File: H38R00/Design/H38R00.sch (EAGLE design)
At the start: 1 part, among them P1 HEXABIT_17.32_X2_POWER_ONLY

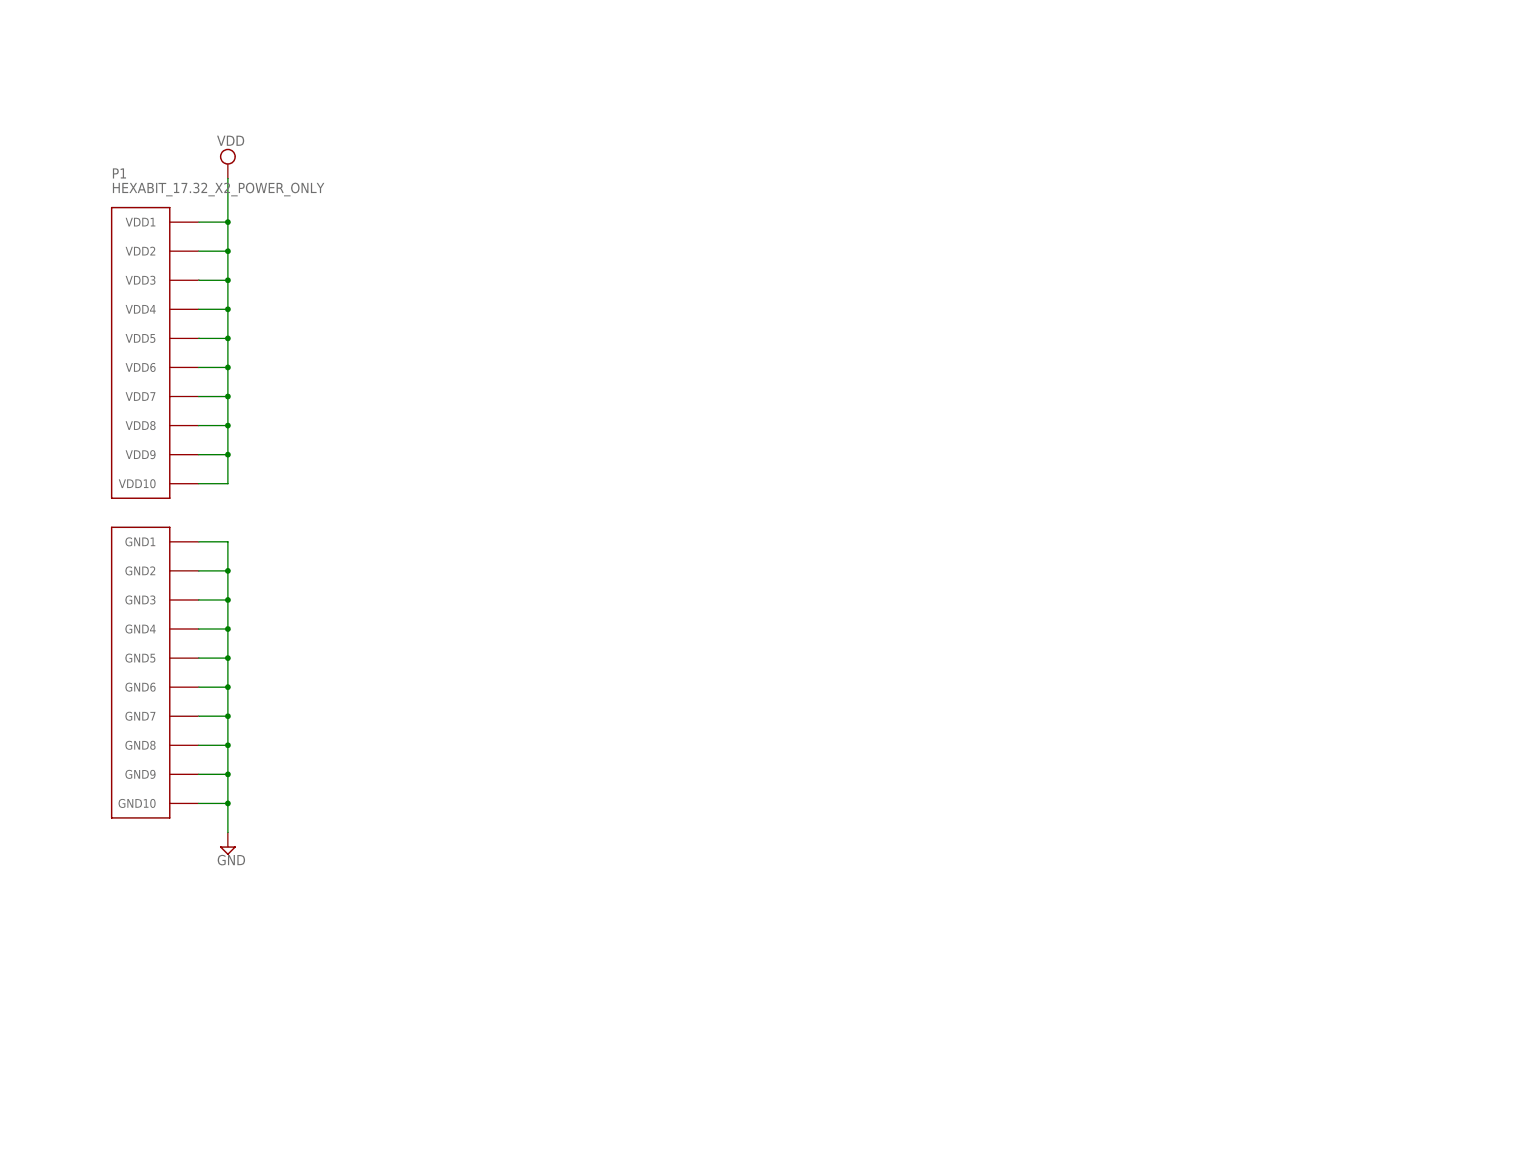
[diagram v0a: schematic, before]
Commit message: Added main ICs and some passives
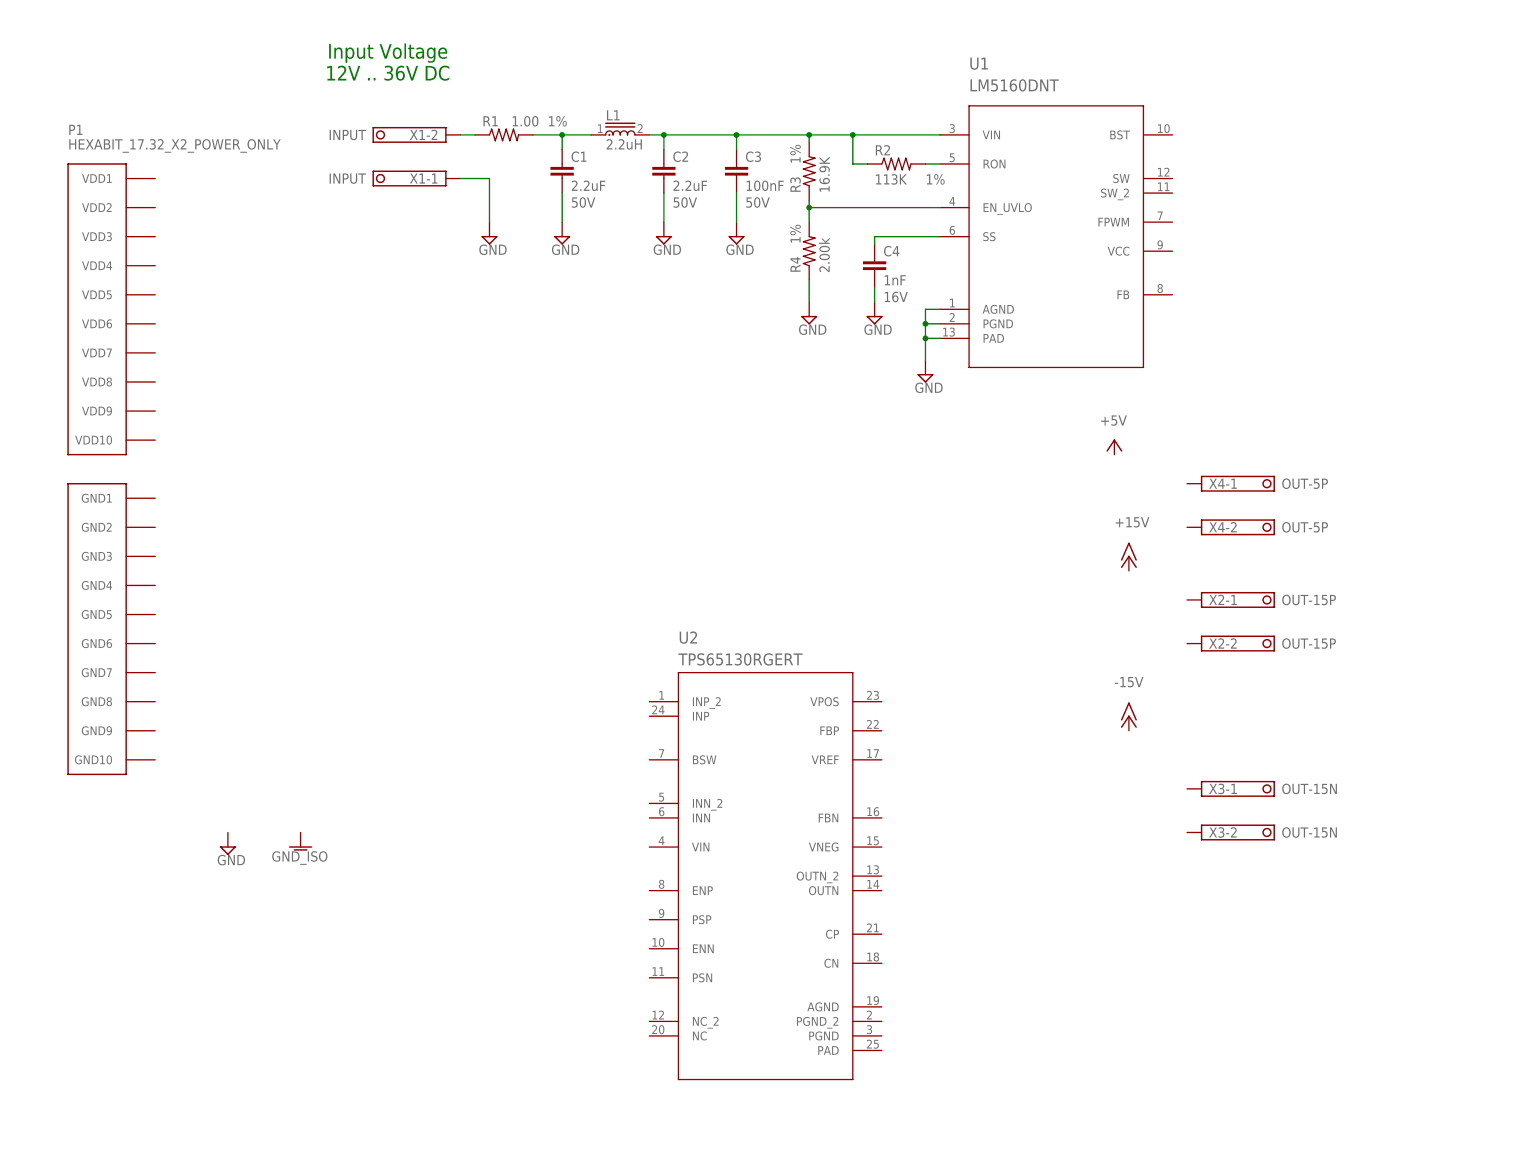
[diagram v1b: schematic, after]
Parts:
- added C1, C2: 2.2uF, Hexabitz:C-1206
- added C3: 100nF, Hexabitz:C-0603
- added C4: 1nF, Hexabitz:C-0603
- added L1: 2.2uH, Hexabitz:LQM18PN2R2MFHD
- added R1: 1.00, Hexabitz:R-0603
- added R2: 113K, Hexabitz:R-0603
- added R3: 16.9K, Hexabitz:R-0603
- added R4: 2.00k, Hexabitz:R-0603
- added U1: LM5160DNT, Hexabitz:LM5160DNT
- added U2: TPS65130RGERT, Hexabitz:TPS65130RGERT
- added X1: INPUT, Hexabitz:CON-PHOENIX-350_1751248
- added X2: OUT-15P, Hexabitz:CON-PHOENIX-350_1751248
- added X3: OUT-15N, Hexabitz:CON-PHOENIX-350_1751248
- added X4: OUT-5P, Hexabitz:CON-PHOENIX-350_1751248
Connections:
- removed net VDD: P1.VDD1, P1.VDD10, P1.VDD2, P1.VDD3, P1.VDD4, P1.VDD5, P1.VDD6, P1.VDD7, P1.VDD8, P1.VDD9
- new net N$1: R1.1, X1-2.K
- new net N$2: C1.1, L1.1, R1.2
- new net N$3: C2.1, C3.1, L1.2, R2.1, R3.2, U1.VIN
- new net N$4: R2.2, U1.RON
- new net N$5: R3.1, R4.2, U1.EN_UVLO
- new net N$6: C4.1, U1.SS
- net GND: now also C1.2, C2.2, C3.2, C4.2, R4.1, U1.AGND, U1.PAD, U1.PGND, X1-1.K; no longer P1.GND1, P1.GND10, P1.GND2, P1.GND3, P1.GND4, P1.GND5, P1.GND6, P1.GND7, P1.GND8, P1.GND9
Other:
- note added: "Input Voltage 12V .. 36V DC"
- note added: "Isolated +/-15V DC-DC Power"
- note removed: "Bipolar +/-15V DC-DC Power"
- moved on the sheet: P1

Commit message: Finished the buck part
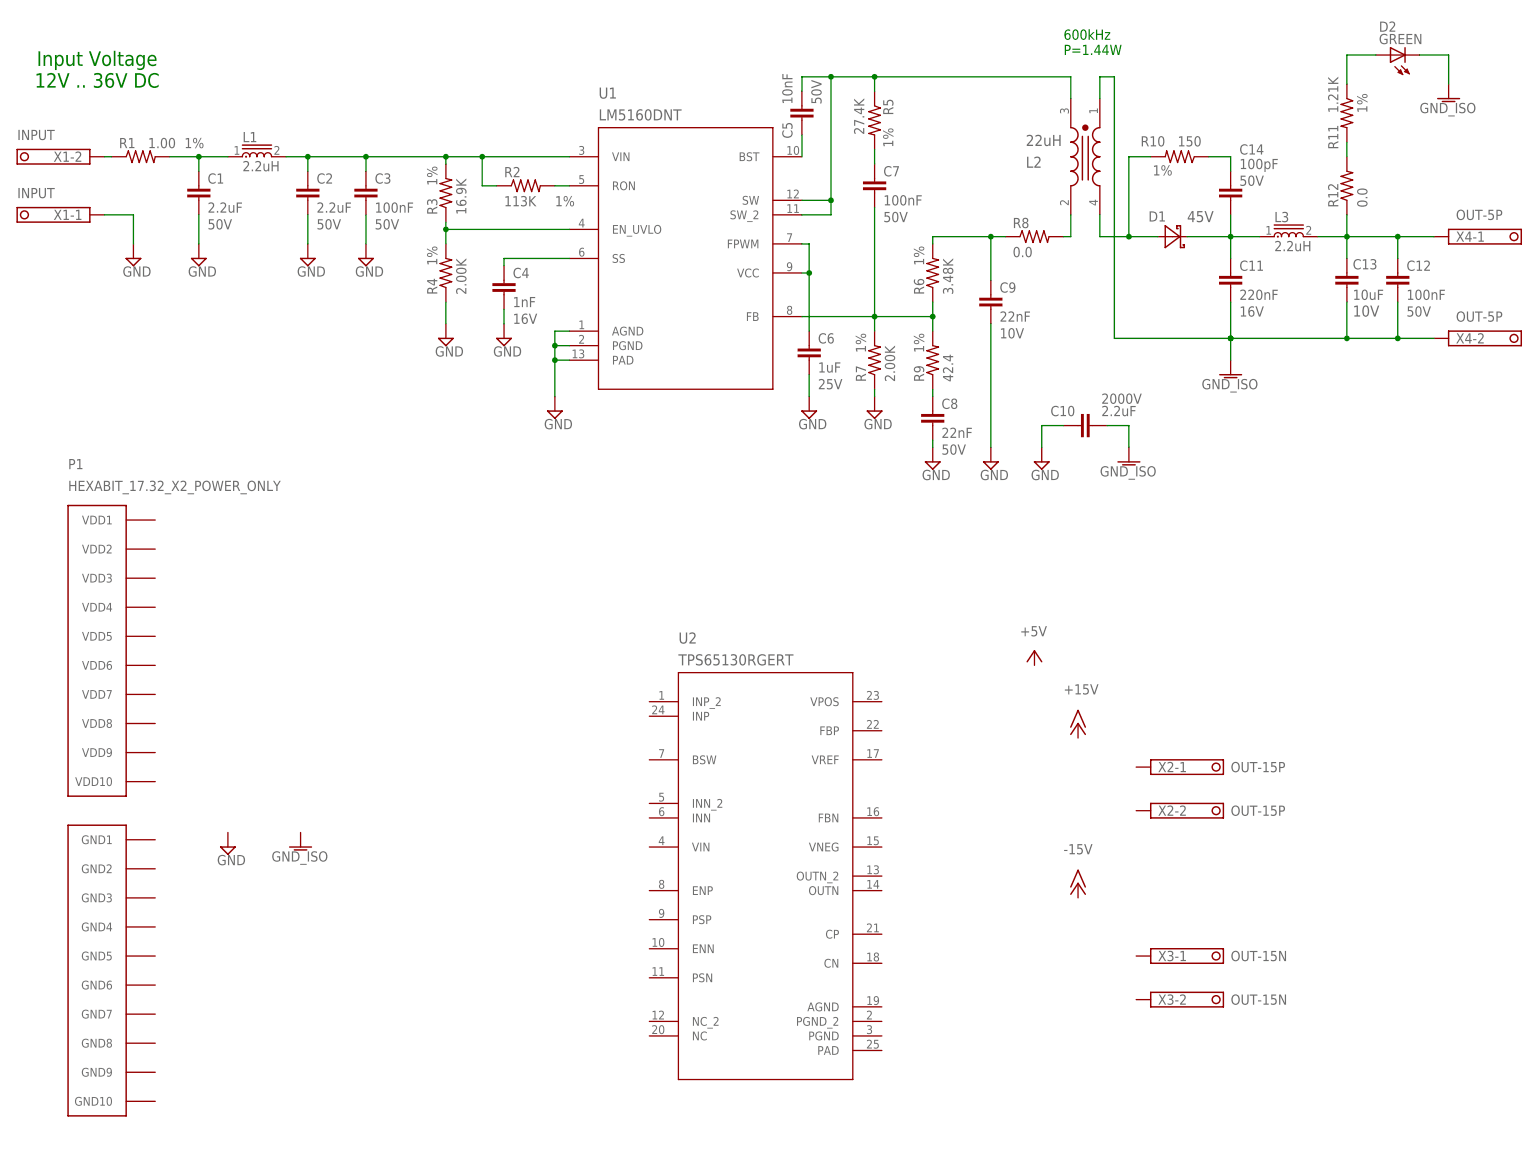
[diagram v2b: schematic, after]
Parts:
- added C10: 2.2uF, Hexabitz:C-1206
- added C11: 220nF, Hexabitz:C-0603
- added C12, C7: 100nF, Hexabitz:C-0603
- added C13: 10uF, Hexabitz:C-0805
- added C14: 100pF, Hexabitz:C-0603
- added C5: 10nF, Hexabitz:C-0603
- added C6: 1uF, Hexabitz:C-0603
- added C8, C9: 22nF, Hexabitz:C-0603
- added D1: DIOD-SOD-123, Hexabitz:DIOD-SOD-123
- added D2: GREEN, Hexabitz:VLMTG1300-GS08
- added L2: 22uH, Hexabitz:WUERTH_ELEKTRONIK_74489430220WUERTH_ELEKTRONIK_74489430220_0_0
- added L3: 2.2uH, Hexabitz:LQM18PN2R2MFHD
- added R10: 150, Hexabitz:R-0603
- added R11: 1.21K, Hexabitz:R-0603
- added R12, R8: 0.0, Hexabitz:R-0603
- added R5: 27.4K, Hexabitz:R-0603
- added R6: 3.48K, Hexabitz:R-0603
- added R7: 2.00K, Hexabitz:R-0603
- added R9: 42.4, Hexabitz:R-0603
- R4: value 2.00k -> 2.00K
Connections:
- new net AGND: C10.2, C11.2, C12.2, C13.2, D2.C, L2.1, X4-2.K
- new net N$10: C7.2, R6.1, R7.2, R9.2, U1.FB
- new net N$11: C7.1, R5.2
- new net N$12: C9.1, R6.2, R8.1
- new net N$13: L2.2, R8.2
- new net N$14: C8.1, R9.1
- new net N$15: C11.1, C14.2, D1.C, L3.1
- new net N$16: D1.A, L2.4, R10.2
- new net N$17: C14.1, R10.1
- new net N$18: C12.1, C13.1, L3.2, R12.1, X4-1.K
- new net N$19: R11.2, R12.2
- new net N$20: D2.A, R11.1
- new net N$7: C5.2, L2.3, R5.1, U1.SW, U1.SW_2
- new net N$8: C5.1, U1.BST
- new net N$9: C6.1, U1.FPWM, U1.VCC
- net GND: now also C10.1, C6.2, C8.2, C9.2, R7.1
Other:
- note added: "600kHz P=1.44W"
- moved on the sheet: C1, C2, C3, C4, L1, P1, R1, R2, R3, R4, U1, X1-1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

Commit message: Finished schematics
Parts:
- added C15, C24, C25, C26, C27: 10uF, Hexabitz:C-0805
- added C16, C17, C20, C21: 100nF, Hexabitz:C-0603
- added C18: 4700pF, Hexabitz:C-0603
- added C19: 10nF, Hexabitz:C-0603
- added C22, C23: 1uF, Hexabitz:C-0603
- added C28: 5.6pF, Hexabitz:C-0603
- added C29: 220nF, Hexabitz:C-0603
- added C30: 6.8pF, Hexabitz:C-0603
- added D3, D4: DIOD-SOD-123, Hexabitz:DIOD-SOD-123
- added D5, D6: GREEN, Hexabitz:VLMTG1300-GS08
- added FB1: 600 Ohm, Hexabitz:FB-0603
- added L4, L5: 10uH, Hexabitz:WUERTH_ELEKTRONIK_74404024100WUERTH_ELEKTRONIK_74404024100_0_0
- added R13: 100.0, Hexabitz:R-0603
- added R14, R15: 1.00, Hexabitz:R-0603
- added R16: 1.30M, Hexabitz:R-0603
- added R17: 86.6K, Hexabitz:R-0603
- added R18: 976K, Hexabitz:R-0603
- added R19, R20: 5.36K, Hexabitz:R-0603
- added SJ1, SJ2, SJ3: (no value), jumper:SJ
- R12: value 0.0 -> 105K; MFN Panasonic -> Vishay; MPN ERJ-3GEY0R00V -> CRCW0603105KFKEA; OCTOPART_URL https://octopart.com/erj-3gey0r00v-panasonic-55389238?r=sp&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 -> https://octopart.com/crcw0603105kfkea-vishay-39783419?r=sp&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; RESISTANCE 0.0R -> 105K; TOLERANCE 5% -> 1%
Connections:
- new net +15V: C24.1, C25.1, R14.2, SJ2.1, X2-1.K
- new net +5V: C12.1, C13.1, FB1.1, L3.2, SJ1.1, X4-1.K
- new net -15V: C26.2, C27.2, R15.2, SJ3.2, X3-2.K
- new net N$21: D3.A, L4.2, U2.INP, U2.INP_2
- new net N$22: C21.1, C23.1, C30.2, D3.C, R14.1, R18.1, U2.VPOS
- new net N$23: C17.1, R13.1, U2.ENN, U2.ENP, U2.PSN, U2.PSP, U2.VIN
- new net N$24: C18.1, U2.CN
- new net N$25: C19.1, U2.CP
- new net N$26: D4.C, L5.1, U2.OUTN, U2.OUTN_2
- new net N$27: C20.2, C22.2, C28.2, D4.A, R15.1, R16.1, U2.VNEG
- new net N$28: C28.1, R12.1, R16.2, U2.FBN
- new net N$29: C29.1, R12.2, U2.VREF
- new net N$30: C30.1, R17.2, R18.2, U2.FBP
- new net N$31: R19.1, SJ2.2
- new net N$32: D5.A, R19.2
- new net N$33: R20.1, SJ3.1
- new net N$34: D6.C, R20.2
- net AGND: now also C15.2, C16.2, C17.2, C18.2, C19.2, C20.1, C21.2, C22.1, C23.2, C24.2, C25.2, C26.1, C27.1, C29.2, D5.C, D6.A, L5.2, R17.1, U2.AGND, U2.PAD, U2.PGND, U2.PGND_2, X2-2.K, X3-1.K
- net N$18: now also C15.1, C16.1, FB1.2, L4.1, R13.2, U2.INN, U2.INN_2; no longer C12.1, C13.1, L3.2, R12.1, X4-1.K
- net N$19: now also SJ1.2; no longer R12.2
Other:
- note added: "+15V"
- note added: "+5V"
- note added: "-15V"
- note added: "Output Voltages"
- moved on the sheet: D2, P1, R11, R12, U2, X2-1, X2-2, X3-1, X3-2
